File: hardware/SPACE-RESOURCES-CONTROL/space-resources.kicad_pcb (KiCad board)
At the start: 4 copper layers, 106.9 x 72 mm, 66 parts, among them J1 XT90 IN, J11 OQ0232510000G, J13 OQ0232510000G, J14 OQ0232510000G, J15 OQ0232510000G, J2 XT30PW-F, J3 OQ0332510000G, J4 OQ0232510000G, J6 OQ0232510000G, J9 Smol_Brain_Board, Q1 CSD19502Q5B, Q2 CSD19502Q5B, U1 LTC4368CMS-1-PBF, U2 INA238, U4 DRV8874PWPR

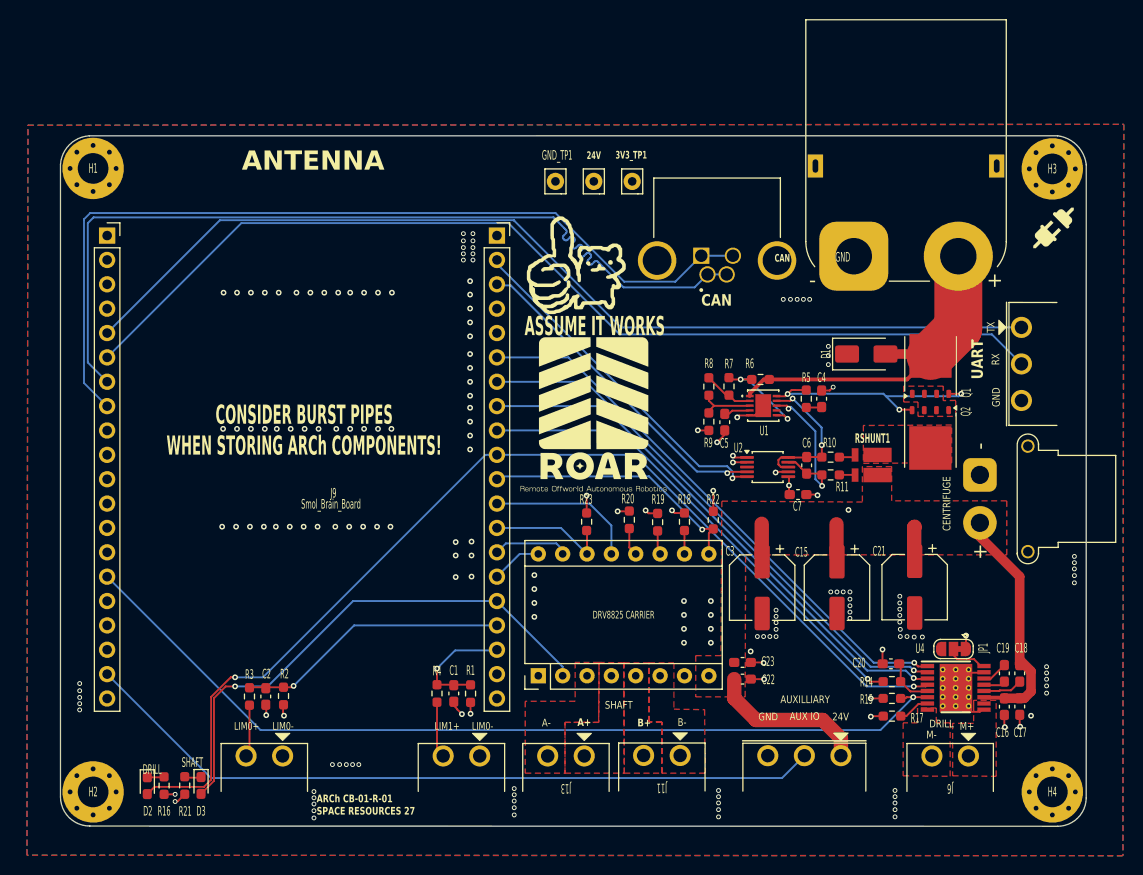
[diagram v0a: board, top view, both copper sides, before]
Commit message: changed dimensions to w x l = 98.9 x 72mm, changed PCB stackup to regular (no add. copper)
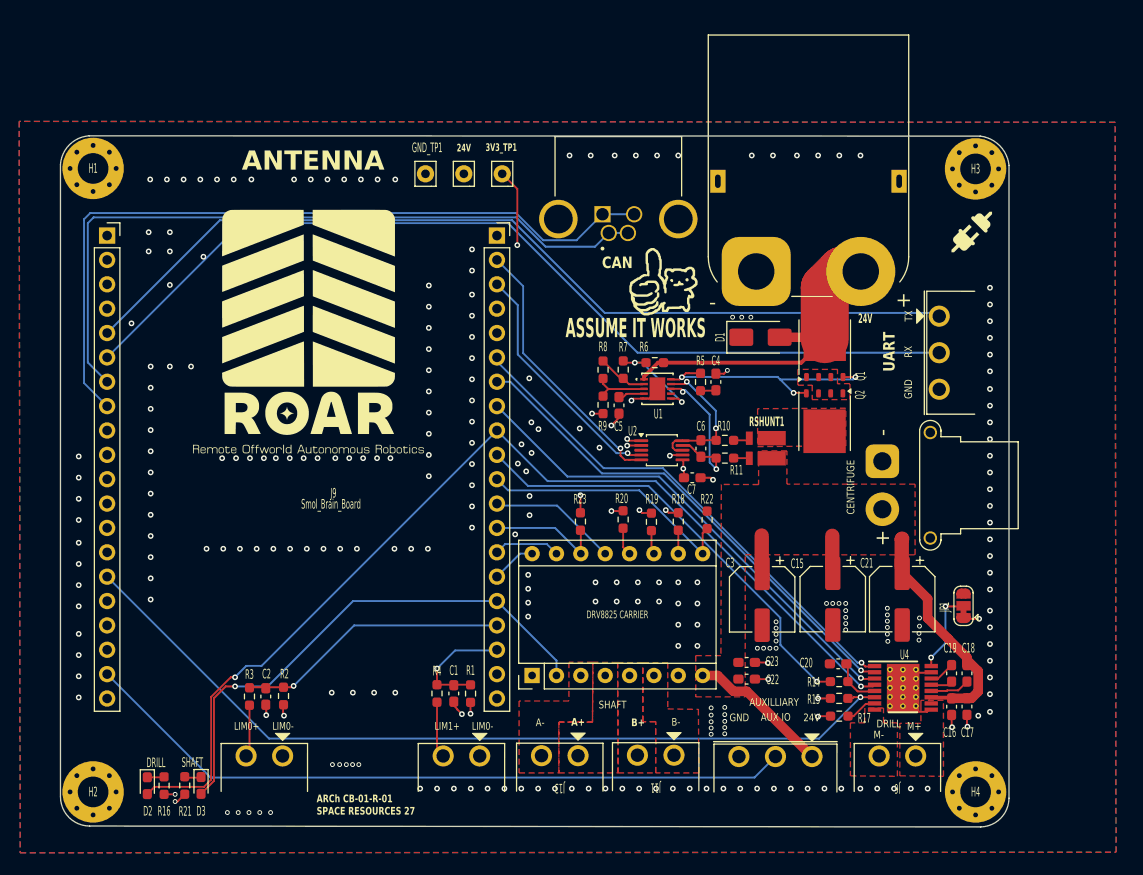
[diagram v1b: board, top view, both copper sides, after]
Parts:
- moved 24V_TP1 13.6 mm to (170.7, 42.9)
- moved 3V3_TP1 13.6 mm to (174.7, 42.9)
- moved GND_TP1 13.6 mm to (166.7, 42.9)
- moved J10 11.2 mm to (186.8, 47.6)
- moved C5 11.2 mm to (186.8, 67.0)
- moved D1 11.2 mm to (201.6, 59.9)
- moved Q1 11.2 mm to (208.3, 61.2)
- moved Q2 11.2 mm to (208.3, 68.7)
- moved R5 11.2 mm to (195.3, 64.6)
- moved R6 11.2 mm to (190.6, 62.6)
- moved R8 11.2 mm to (185.2, 63.3)
- moved R9 11.2 mm to (185.2, 67.0)
- moved RSHUNT1 11.2 mm to (202.1, 71.5)
- moved U1 11.2 mm to (190.8, 65.3)
- moved U2 11.2 mm to (191.3, 71.7)
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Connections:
- J9 pad 31: /~{DRL_FAULT} -> /DRL_I_LIM
- J9 pad 32: /DRL_I_LIM -> /~{DRL_FAULT}
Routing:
- net /CAN_H+: track 92.8 -> 75.8 mm
- net +3V3: track 163.8 -> 148.3 mm, vias 7 -> 8
- net /CAN_L-: track 92.5 -> 80.4 mm
- net /UART1_TX: track 104.8 -> 95.8 mm
- net /UART1_RX: track 107.2 -> 98.1 mm, vias 0 -> 1
- net /I2C_SDA: track 34.3 -> 25.4 mm
- net /I2C_SCK: track 36.3 -> 28.6 mm
- net /~{DRL_SLEEP}: track 56.7 -> 51.1 mm
- net /DRL_IN2: track 57.4 -> 51.9 mm
- net /DRL_IN1: track 58.1 -> 52.9 mm
- net /DRL_I_LIM: track 51.1 -> 46.2 mm
- net /MOT_ISNS: track 94.4 -> 89.6 mm
- net Net-(JP1-C): track 4.04 -> 8.75 mm, vias 0 -> 2
- net +24V_unprot: track 39.9 -> 35.7 mm
- net +24V_prot: track 158.2 -> 161.7 mm, vias 1 -> 0
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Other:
- board size 106.9 x 72 mm -> 98.9 x 72.1 mm
- board text added: "U4"
